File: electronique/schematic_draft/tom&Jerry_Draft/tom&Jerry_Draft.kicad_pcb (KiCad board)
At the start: 4 copper layers, 54 x 57 mm, 166 parts, among them IC1001 NCS199A2RSQT2G, IC301 TCA9555RTWR, IC901 NCS199A2RSQT2G, J1201 Conn_01x02, J1301 Conn_01x02, J1401 Conn_01x02, J1501 Conn_01x02, J1601 Conn_02x05_Odd_FEMALE, J1602 Conn_02x05_Odd_FEMALE, J1603 Conn_02x05_Odd_FEMALE, J201 Conn_01x02, J202 USB_C_Receptacle_USB2.0_16P, J203 Conn_01x02, J204 Interrupteur, J301 FTSH-105-01-F-DV-P-TR, J302 FTSH-105-01-F-DV-P-TR, J303 FTSH-105-01-F-DV-P-TR, J304 FTSH-105-01-F-DV-P-TR, J305 Conn_01x08, J401 Conn_01x06, J402 Conn_01x06, J501 Conn_ST_STDC14, J601 Conn_01x03, J701 Conn_02x05_Odd_FEMALE, J702 Conn_02x05_Odd_FEMALE, J703 Conn_02x05_Odd_FEMALE, Q201 PMOS, SW501 SW_Push, SW502 SW_Push, SW503 SW_Push, U1001 ZXBM5210-S, U201 MP1475DJ-LF-P, U202 BQ25172DSGR, U301 ADXL343, U501 STM32G431CBU6, U601 PAM8302AAY, U801 LP5812ADSDR, U901 ZXBM5210-S, Y501 16MHz

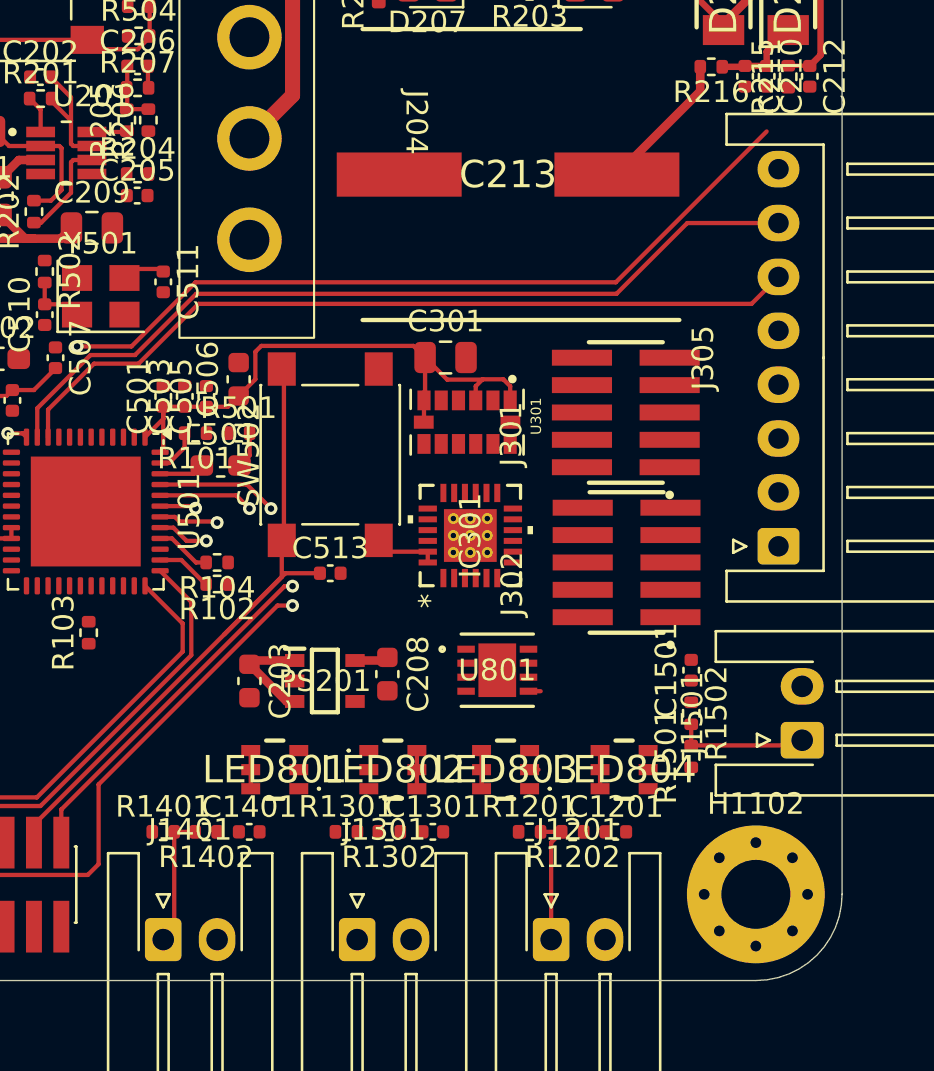
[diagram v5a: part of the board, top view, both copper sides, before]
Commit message: Ajout du routage LED + TOF + quelques Via
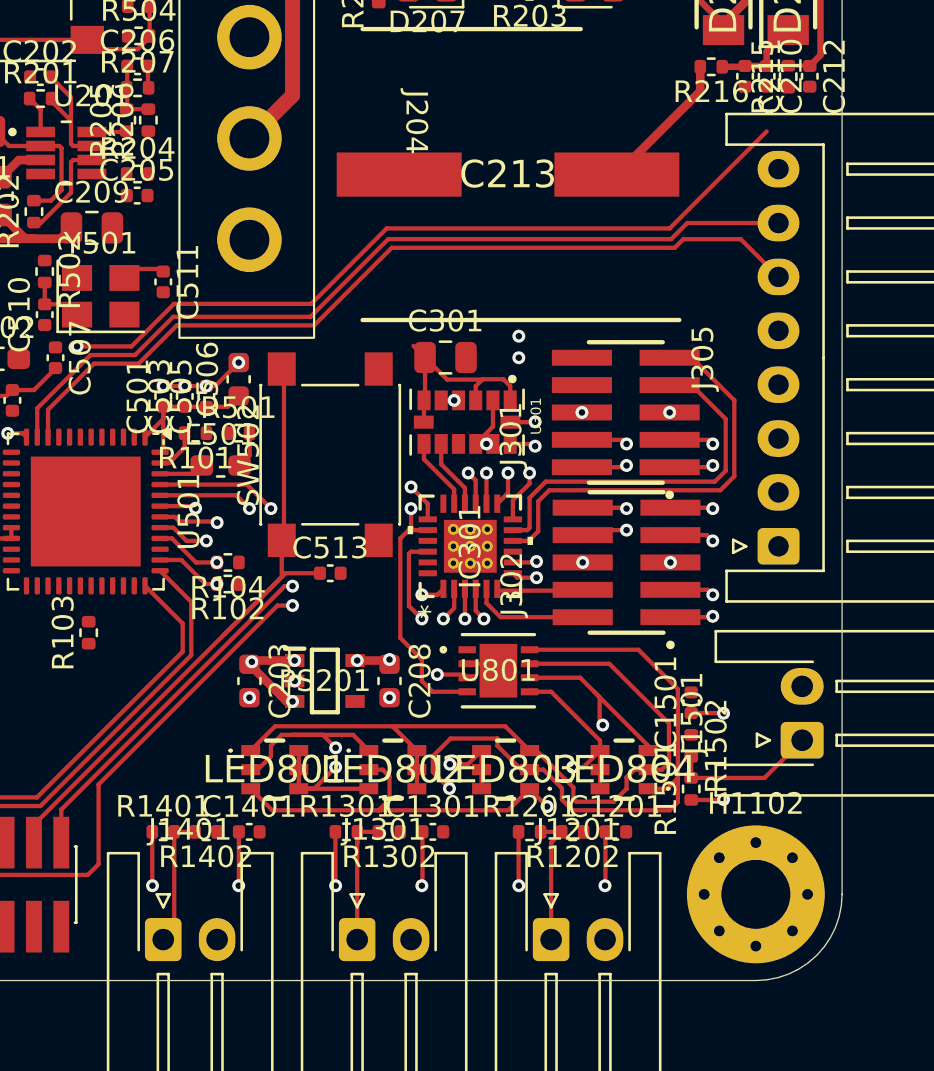
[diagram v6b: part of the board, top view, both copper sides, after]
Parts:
- moved C1501 1.51 mm to (121.0, 101.5)
- moved R1501 1.51 mm to (121.0, 105.5)
- moved R1502 1.51 mm to (121.0, 103.5)
- moved IC301 0.50 mm to (110.8, 94.2)
- moved R102 0.50 mm to (99.5, 96.0)
- moved R104 0.50 mm to (99.5, 95.0)
- moved C208 0.34 mm to (107.0, 100.5)
- moved U801 0.06 mm to (112.1, 100.0)
- turned LED801 to 0 degrees
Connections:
- IC301 pad 1: /Périphériques/TOF6_XSHUT -> /Périphériques/TOF4_XSHUT
- IC301 pad 12: /Périphériques/TOF1_GPIO1 -> /Périphériques/TOF3_XSHUT
- IC301 pad 13: /Périphériques/TOF1_XSHUT -> /Périphériques/TOF3_GPIO1
- IC301 pad 14: /Périphériques/IMU_INT1 -> /Périphériques/LIDAR_M_EN
- IC301 pad 15: /Périphériques/IMU_INT2 -> /Périphériques/LIDAR_DEV_EN
- IC301 pad 16: /Périphériques/LIDAR_M_EN -> /Périphériques/IMU_INT2
- IC301 pad 17: /Périphériques/LIDAR_DEV_EN -> /Périphériques/IMU_INT1
- IC301 pad 2: /Périphériques/TOF6_GPIO1 -> /Périphériques/TOF4_GPIO1
- IC301 pad 5: /Périphériques/TOF4_XSHUT -> /Périphériques/TOF6_XSHUT
- IC301 pad 6: /Périphériques/TOF4_GPIO1 -> /Périphériques/TOF6_GPIO1
- IC301 pad 7: /Périphériques/TOF3_GPIO1 -> /Périphériques/TOF1_GPIO1
- IC301 pad 8: /Périphériques/TOF3_XSHUT -> /Périphériques/TOF1_XSHUT
- J302 pad 02: /Led_Debug/Led_Debug_SCL -> /Périphériques/TOF6_XSHUT
- J302 pad 04: /Led_Debug/Led_Debug_SDA -> /Périphériques/TOF6_GPIO1
- J302 pad 08: /Périphériques/TOF6_GPIO1 -> /Led_Debug/Led_Debug_SCL
- J302 pad 10: /Périphériques/TOF6_XSHUT -> /Led_Debug/Led_Debug_SDA
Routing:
- net Net-(LED801-B-): track 2.19 -> 37.6 mm, vias 0 -> 2
- net Net-(LED801-R+): track 1.77 -> 35.5 mm
- net Net-(LED801-B+): track 2.34 -> 25.8 mm, vias 0 -> 2
- net /Périphériques/TOF2_GPIO1: track 0.00 -> 19.7 mm
- net Net-(LED801-G+): track 1.77 -> 21.2 mm, vias 0 -> 3
- net /Périphériques/TOF2_XSHUT: track 0.00 -> 17.5 mm
- net /Led_Debug/Led_Debug_SDA: track 2.60 -> 19.1 mm, vias 0 -> 4
- net +3.3V: track 32.5 -> 23.0 mm, vias 0 -> 2
- net /Led_Debug/Led_Debug_SCL: track 0.00 -> 7.50 mm, vias 0 -> 4
- net GND: track 2.99 -> 10.2 mm, vias 0 -> 11
- net Net-(J1301-Pin_1): track 0.00 -> 5.97 mm
- net /Périphériques/TOF6_XSHUT: track 0.00 -> 5.40 mm
- net /Périphériques/MOUSTACHE_2: track 0.00 -> 5.02 mm, vias 0 -> 2
- net /Périphériques/MOUSTACHE_1: track 0.00 -> 5.01 mm, vias 0 -> 2
- net /Périphériques/MOUSTACHE_3: track 0.00 -> 5.01 mm, vias 0 -> 2
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
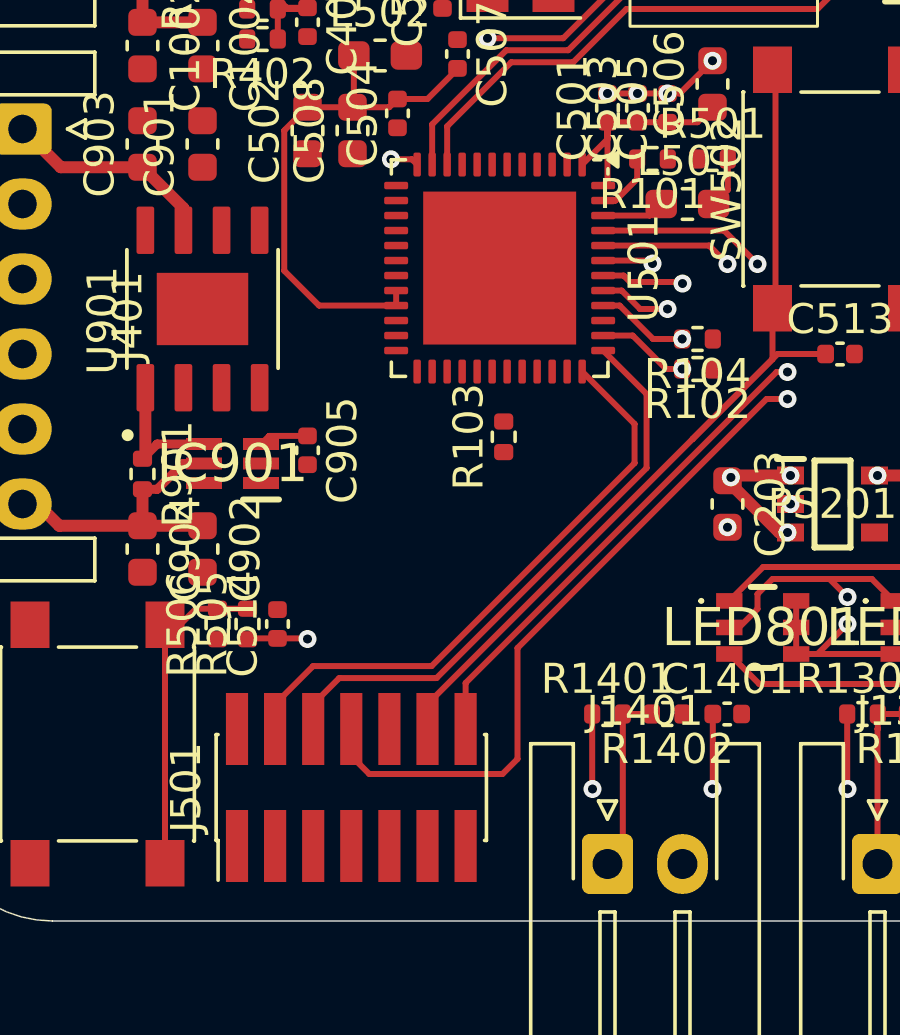
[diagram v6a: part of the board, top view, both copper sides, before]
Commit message: Ajout des derniers via utiles
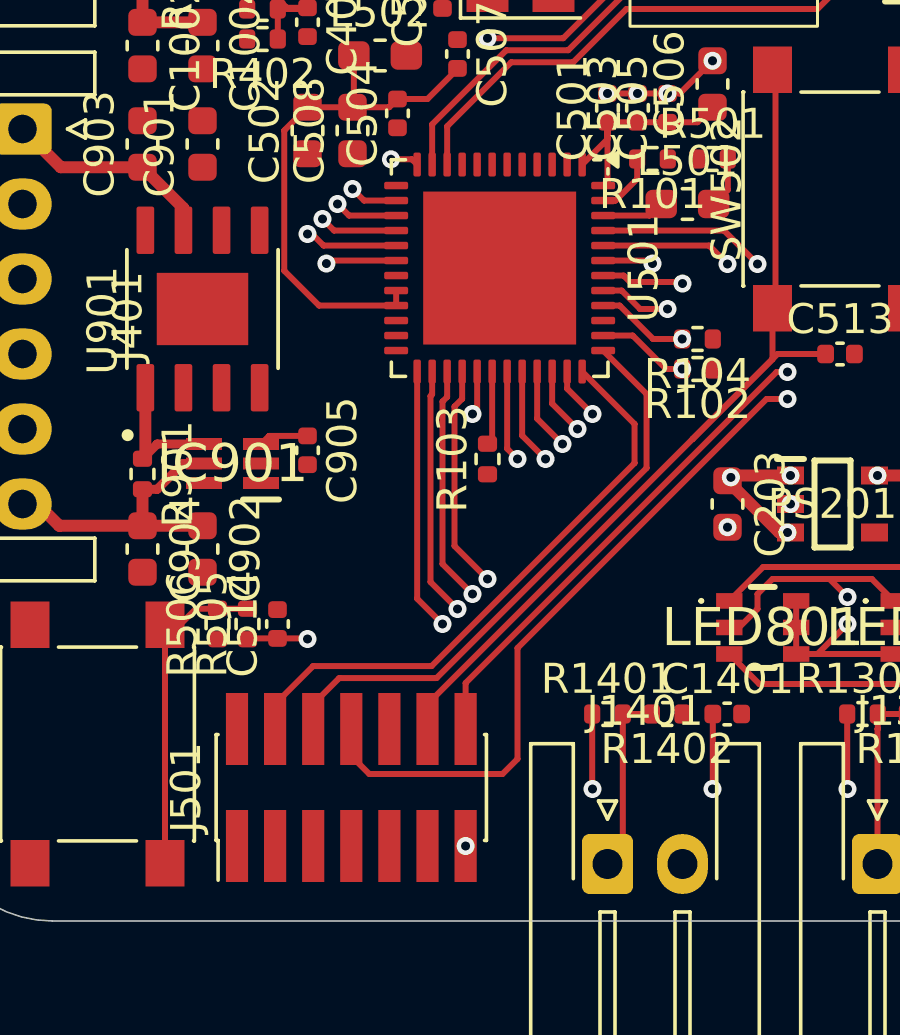
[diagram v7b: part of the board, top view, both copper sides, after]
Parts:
- moved R103 0.92 mm to (92.5, 99.0)
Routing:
- net /Périphériques/MOUSTACHE_4: track 3.01 -> 11.8 mm, vias 2 -> 3
- net /Périphériques/MOUSTACHE_3: track 5.01 -> 13.3 mm, vias 2 -> 3
- net /Périphériques/MOUSTACHE_2: track 5.02 -> 12.9 mm, vias 2 -> 3
- net /Périphériques/MOUSTACHE_1: track 5.01 -> 12.5 mm, vias 2 -> 3
- net /Alimentation/CC1: track 6.24 -> 9.48 mm, vias 2 -> 3
- net /Motors&Drivers/PWM_MOT2_CH1: track 0.00 -> 3.11 mm, vias 0 -> 1
- net /Alimentation/CC2: track 4.93 -> 7.98 mm, vias 2 -> 3
- net /Périphériques/LIDAR_M_CTR: track 0.00 -> 2.77 mm, vias 0 -> 1
- net /STM32/VCP_RX: track 0.00 -> 2.61 mm, vias 0 -> 2
- net /Led_Debug/Led_Debug_SCL: track 7.50 -> 9.97 mm
- net /Motors&Drivers/PWM_MOT2_CH2: track 0.00 -> 2.37 mm, vias 0 -> 1
- net /Périphériques/EXPANDER_EXTI: track 4.18 -> 6.45 mm, vias 1 -> 2
- net /Motors&Drivers/ASSERV_I2: track 0.00 -> 2.11 mm, vias 0 -> 1
- net +3.3V: track 23.0 -> 24.8 mm, vias 2 -> 3
- net /Motors&Drivers/ASSERV_I1: track 0.00 -> 1.61 mm, vias 0 -> 1
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
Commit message: Routage Signal Complet
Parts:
- added H1104: MountingHole_Pad, MountingHole:MountingHole_3.2mm_M3_Pad_Via, F.Cu at (43.2, 40.8)
- added TP201: TestPoint_Small, Test_Point:TestPoint_Pad_D1.5mm, F.Cu at (41.0, 22.4)
- added TP202: TestPoint_Small, Test_Point:TestPoint_Pad_D1.5mm, F.Cu at (41.0, 26.0)
- added TP203: TestPoint_Small, Test_Point:TestPoint_Pad_D1.5mm, F.Cu at (41.0, 29.5)
- added TP204: TestPoint_Small, Test_Point:TestPoint_Pad_D1.5mm, F.Cu at (41.0, 33.1)
- added TP501: PC6, Test_Point:TestPoint_Pad_D1.5mm, F.Cu at (28.4, 22.4)
- added TP502: PB0, Test_Point:TestPoint_Pad_D1.5mm, F.Cu at (28.4, 26.0)
- added TP503: PB1, Test_Point:TestPoint_Pad_D1.5mm, F.Cu at (28.4, 29.5)
- added TP504: PB4, Test_Point:TestPoint_Pad_D1.5mm, F.Cu at (28.4, 33.1)
- added TP505: PB5, Test_Point:TestPoint_Pad_D1.5mm, F.Cu at (28.4, 36.6)
- added TP506: PB6, Test_Point:TestPoint_Pad_D1.5mm, F.Cu at (28.4, 40.2)
- added TP507: PB10, Test_Point:TestPoint_Pad_D1.5mm, F.Cu at (31.9, 22.4)
- added TP508: PB11, Test_Point:TestPoint_Pad_D1.5mm, F.Cu at (31.9, 26.0)
- added TP509: PA0, Test_Point:TestPoint_Pad_D1.5mm, F.Cu at (31.9, 29.5)
- added TP510: PA1, Test_Point:TestPoint_Pad_D1.5mm, F.Cu at (31.9, 33.1)
- added TP511: PA4, Test_Point:TestPoint_Pad_D1.5mm, F.Cu at (31.9, 36.6)
- added TP512: PA6, Test_Point:TestPoint_Pad_D1.5mm, F.Cu at (31.9, 40.2)
- added TP513: PA7, Test_Point:TestPoint_Pad_D1.5mm, F.Cu at (35.5, 22.4)
- added TP514: PA9, Test_Point:TestPoint_Pad_D1.5mm, F.Cu at (35.5, 26.0)
- added TP515: PA10, Test_Point:TestPoint_Pad_D1.5mm, F.Cu at (35.5, 29.5)
- added TP516: PA11, Test_Point:TestPoint_Pad_D1.5mm, F.Cu at (35.5, 33.1)
- added TP517: PA12, Test_Point:TestPoint_Pad_D1.5mm, F.Cu at (35.5, 36.6)
- moved D202 0.33 mm to (95.0, 61.2)
- moved D203 0.33 mm to (93.5, 61.2)
- moved D204 0.33 mm to (96.5, 61.2)
- moved R208 0.33 mm to (95.5, 58.7)
- moved R209 0.33 mm to (93.5, 58.7)
- moved R210 0.33 mm to (97.5, 58.7)
- moved JP203 0.27 mm to (96.8, 64.7)
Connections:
- IC301 pad 1: /Périphériques/TOF4_XSHUT -> /Périphériques/TOF5_XSHUT
- IC301 pad 14: /Périphériques/LIDAR_M_EN -> /Périphériques/LIDAR_DEV_EN
- IC301 pad 15: /Périphériques/LIDAR_DEV_EN -> /Périphériques/LIDAR_M_EN
- IC301 pad 3: /Périphériques/TOF5_XSHUT -> /Périphériques/TOF4_XSHUT
- IC301 pad 7: /Périphériques/TOF1_GPIO1 -> /Périphériques/TOF1_XSHUT
- IC301 pad 8: /Périphériques/TOF1_XSHUT -> /Périphériques/TOF1_GPIO1
- U202 pad 10: (no net) -> GND
- U202 pad 11: (no net) -> GND
- U501 pad 22: /Motors&Drivers/PWM_MOT1_CH1 -> /Motors&Drivers/PWM_MOT1_CH2
- U501 pad 24: /Motors&Drivers/PWM_MOT1_CH2 -> /Motors&Drivers/PWM_MOT1_CH1
- U501 pad 25: /Périphériques/MOUSTACHE_4 -> /Périphériques/MOUSTACHE_3
- U501 pad 26: /Périphériques/MOUSTACHE_3 -> /Périphériques/MOUSTACHE_2
- U501 pad 27: /Périphériques/MOUSTACHE_2 -> /Périphériques/MOUSTACHE_1
- U501 pad 28: /Périphériques/MOUSTACHE_1 -> /Périphériques/MOUSTACHE_4
- U501 pad 8: /Motors&Drivers/ENCODER_1A -> /Motors&Drivers/ENCODER_1B
- U501 pad 9: /Motors&Drivers/ENCODER_1B -> /Motors&Drivers/ENCODER_1A
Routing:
- net GND: track 10.2 -> 101.1 mm, vias 11 -> 49
- net /Motors&Drivers/ENCODER_2B: track 1.69 -> 78.9 mm
- net /Motors&Drivers/ENCODER_1A: track 0.00 -> 55.2 mm, vias 0 -> 1
- net /Motors&Drivers/ENCODER_1B: track 0.00 -> 53.8 mm, vias 0 -> 1
- net /Alimentation/CC2: track 7.98 -> 59.2 mm
- net /Alimentation/CC1: track 9.48 -> 58.6 mm
- net /Périphériques/LIDAR_M_CTR: track 2.77 -> 46.0 mm
- net /Périphériques/MOUSTACHE_4: track 11.8 -> 47.5 mm
- net /STM32/VCP_RX: track 2.61 -> 36.6 mm
- net /Motors&Drivers/ENCODER_2A: track 1.48 -> 34.3 mm
- net /Led_Debug/Led_Debug_SCL: track 9.97 -> 39.4 mm
- net /Périphériques/MOUSTACHE_1: track 12.5 -> 40.6 mm
- net /Motors&Drivers/PWM_MOT2_CH2: track 2.37 -> 29.8 mm, vias 1 -> 2
- net /STM32/BUTTON_Initial_State: track 1.14 -> 25.7 mm, vias 0 -> 2
- net /STM32/BUTTON_Start_Robot: track 2.02 -> 24.8 mm, vias 1 -> 2
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- added copper zone on F.Cu, net +3.3V
- added copper zone on F.Cu, net GND
